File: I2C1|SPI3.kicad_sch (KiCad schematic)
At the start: 6 parts, among them U16 ZX-SH1.0-4PWT, U19 ZX-SH1.0-6PWT

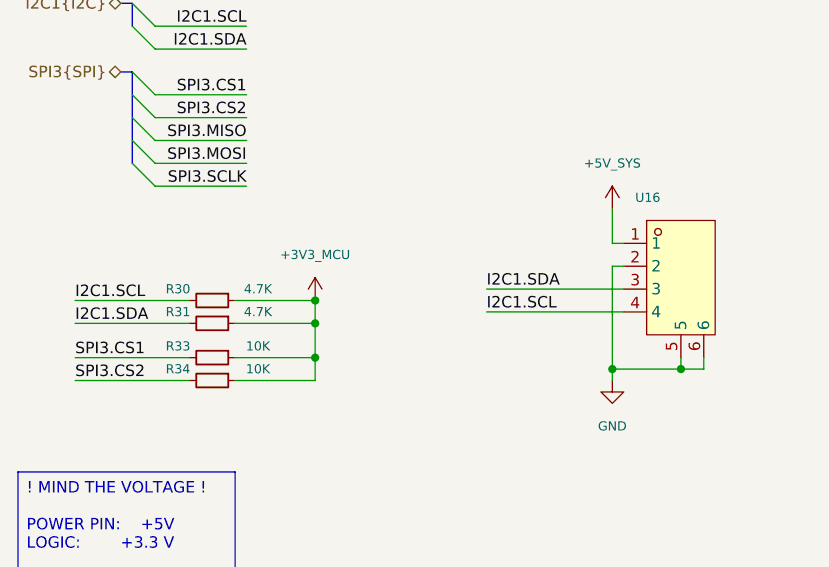
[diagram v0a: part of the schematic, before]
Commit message: grouped ICs and passives
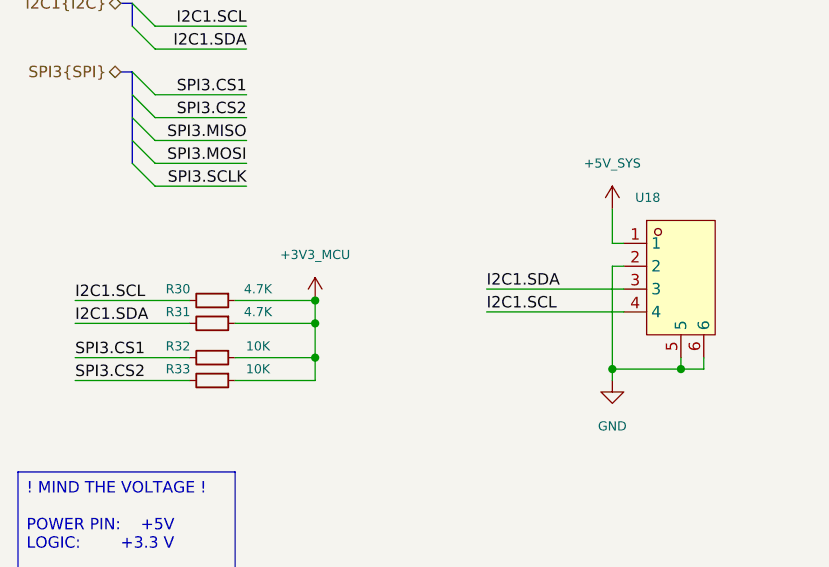
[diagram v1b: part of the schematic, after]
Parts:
- renumbered R33 to R32, R34 to R33, U16 to U18
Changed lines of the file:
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@@
 		(in_pos_files yes)
 		(dnp no)
-		(property "Reference" "R34"
+		(property "Reference" "R33"
 			(at 34.29 72.39 90)
 			(show_name no)
@@
 			(project "LEVIA_H7"
 				(path "/6b768b36-fce6-4be0-9021-6d41bddc3a70/63f0a0da-13f8-4f9f-a395-c486a2aaa319"
-					(reference "R34")
+					(reference "R33")
 					(unit 1)
 				)
@@
 		(dnp no)
 		(fields_autoplaced yes)
-		(property "Reference" "#PWR086"
+		(property "Reference" "#PWR0107"
 			(at 138.43 58.42 0)
 			(hide yes)
@@
 			(project "LEVIA_H7"
 				(path "/6b768b36-fce6-4be0-9021-6d41bddc3a70/63f0a0da-13f8-4f9f-a395-c486a2aaa319"
-					(reference "#PWR086")
+					(reference "#PWR0107")
 					(unit 1)
 				)
@@
 		(in_pos_files yes)
 		(dnp no)
-		(property "Reference" "U16"
+		(property "Reference" "U18"
 			(at 85.09 53.34 0)
 			(show_name no)
@@
 			(project "LEVIA_H7"
 				(path "/6b768b36-fce6-4be0-9021-6d41bddc3a70/63f0a0da-13f8-4f9f-a395-c486a2aaa319"
-					(reference "U16")
+					(reference "U18")
 					(unit 1)
 				)
@@
 		(dnp no)
 		(fields_autoplaced yes)
-		(property "Reference" "#PWR087"
+		(property "Reference" "#PWR0108"
 			(at 138.43 85.09 0)
 			(hide yes)
@@
 			(project "LEVIA_H7"
 				(path "/6b768b36-fce6-4be0-9021-6d41bddc3a70/63f0a0da-13f8-4f9f-a395-c486a2aaa319"
-					(reference "#PWR087")
+					(reference "#PWR0108")
 					(unit 1)
 				)
@@
 		(dnp no)
 		(fields_autoplaced yes)
-		(property "Reference" "#PWR046"
+		(property "Reference" "#PWR0104"
 			(at 49.53 68.58 0)
 			(hide yes)
@@
 			(project "LEVIA_H7"
 				(path "/6b768b36-fce6-4be0-9021-6d41bddc3a70/63f0a0da-13f8-4f9f-a395-c486a2aaa319"
-					(reference "#PWR046")
+					(reference "#PWR0104")
 					(unit 1)
 				)
@@
 		(dnp no)
 		(fields_autoplaced yes)
-		(property "Reference" "#PWR082"
+		(property "Reference" "#PWR0106"
 			(at 82.55 80.01 0)
 			(hide yes)
@@
 			(project "LEVIA_H7"
 				(path "/6b768b36-fce6-4be0-9021-6d41bddc3a70/63f0a0da-13f8-4f9f-a395-c486a2aaa319"
-					(reference "#PWR082")
+					(reference "#PWR0106")
 					(unit 1)
 				)
@@
 		(dnp no)
 		(fields_autoplaced yes)
-		(property "Reference" "#PWR067"
+		(property "Reference" "#PWR0105"
 			(at 82.55 58.42 0)
 			(hide yes)
@@
 			(project "LEVIA_H7"
 				(path "/6b768b36-fce6-4be0-9021-6d41bddc3a70/63f0a0da-13f8-4f9f-a395-c486a2aaa319"
-					(reference "#PWR067")
+					(reference "#PWR0105")
 					(unit 1)
 				)
@@
 		(in_pos_files yes)
 		(dnp no)
-		(property "Reference" "R33"
+		(property "Reference" "R32"
 			(at 34.29 69.85 90)
 			(show_name no)
@@
 			(project "LEVIA_H7"
 				(path "/6b768b36-fce6-4be0-9021-6d41bddc3a70/63f0a0da-13f8-4f9f-a395-c486a2aaa319"
-					(reference "R33")
-					(unit 1)
-				)
+					(reference "R32")
+					(unit 1)
+				)
